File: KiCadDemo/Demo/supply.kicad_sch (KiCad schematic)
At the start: 13 parts, among them J1 Power, U1 TSR_1-2450, U2 UA78M33

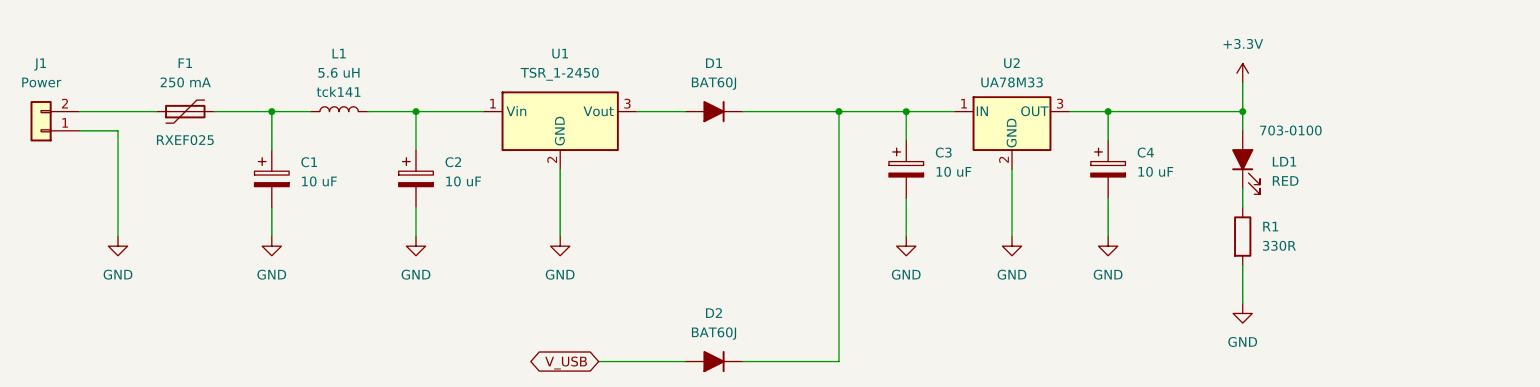
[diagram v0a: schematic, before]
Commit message: Footprints check 3
Added "Power" footprint, and "IO2" not completed.
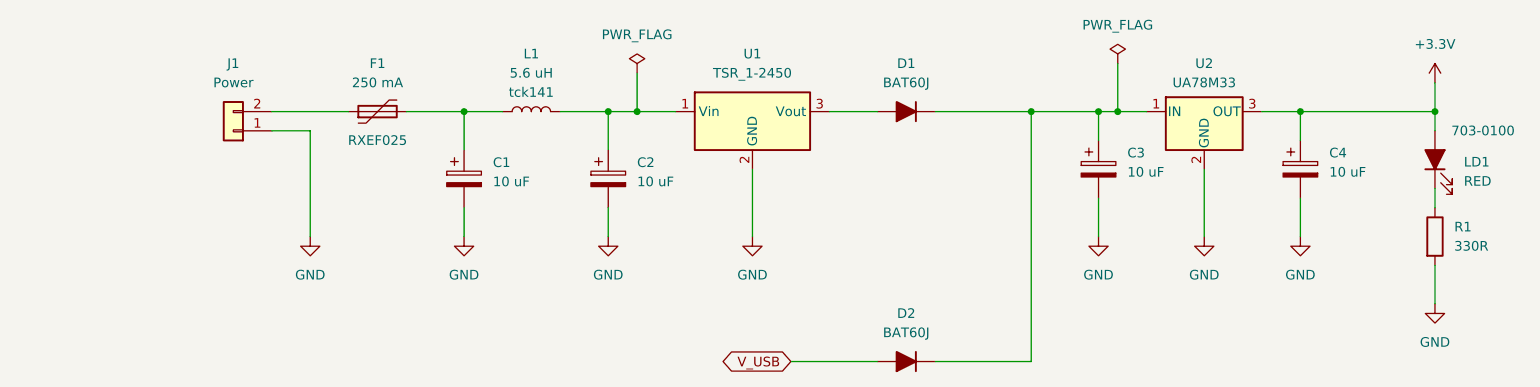
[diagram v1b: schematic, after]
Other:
- moved on the sheet: C1, C2, C3, C4, D1, D2, F1, J1, L1, LD1, R1, U1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
